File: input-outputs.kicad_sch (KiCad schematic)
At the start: 5 parts, among them J5 I2C-STEMMA-QT, J7 swd, J9 UART

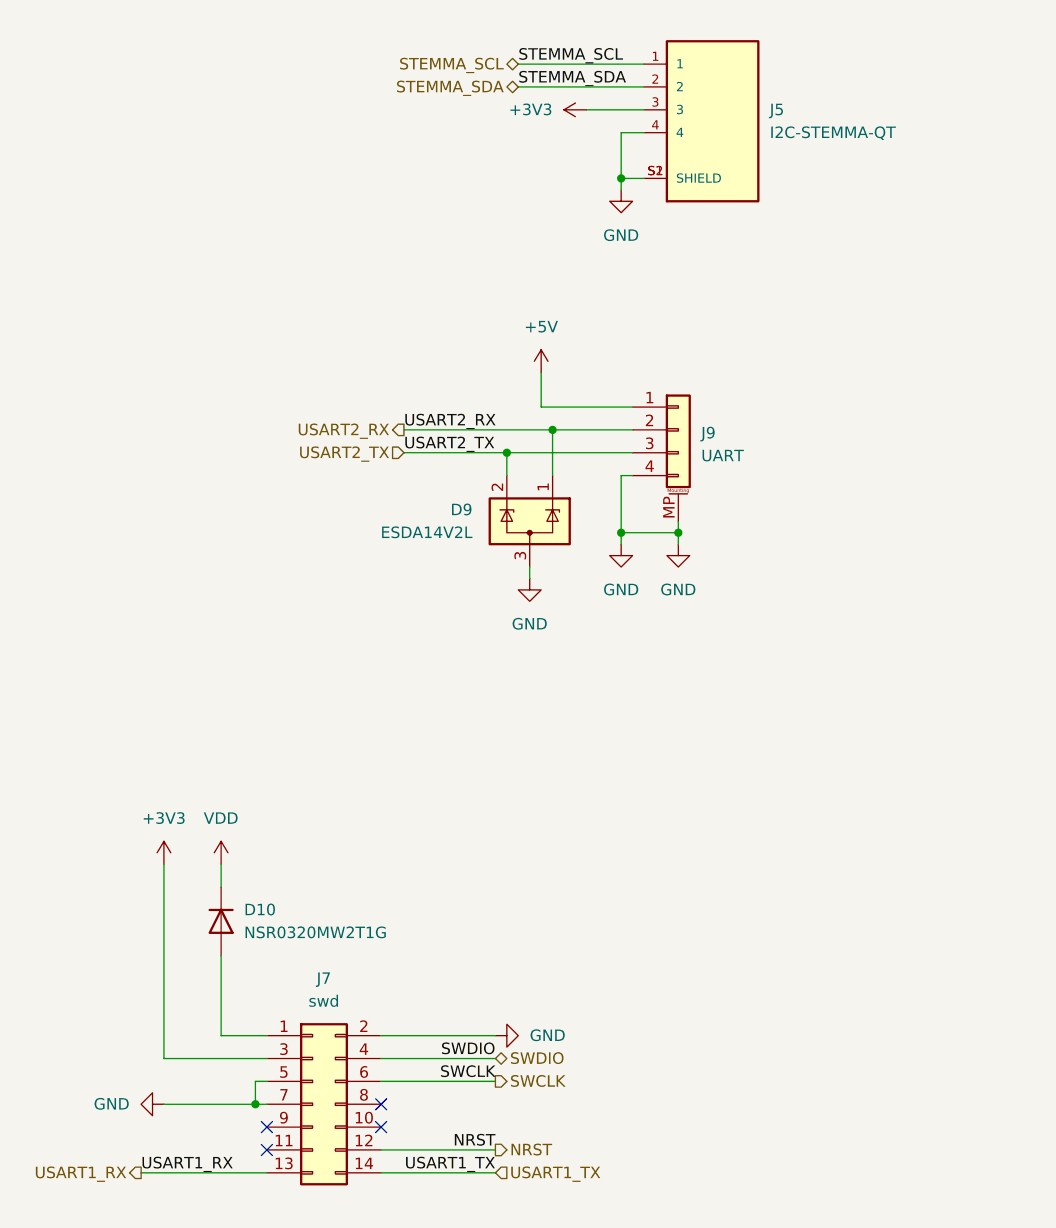
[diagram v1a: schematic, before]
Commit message: Cleaning schematic, added more independently schematics
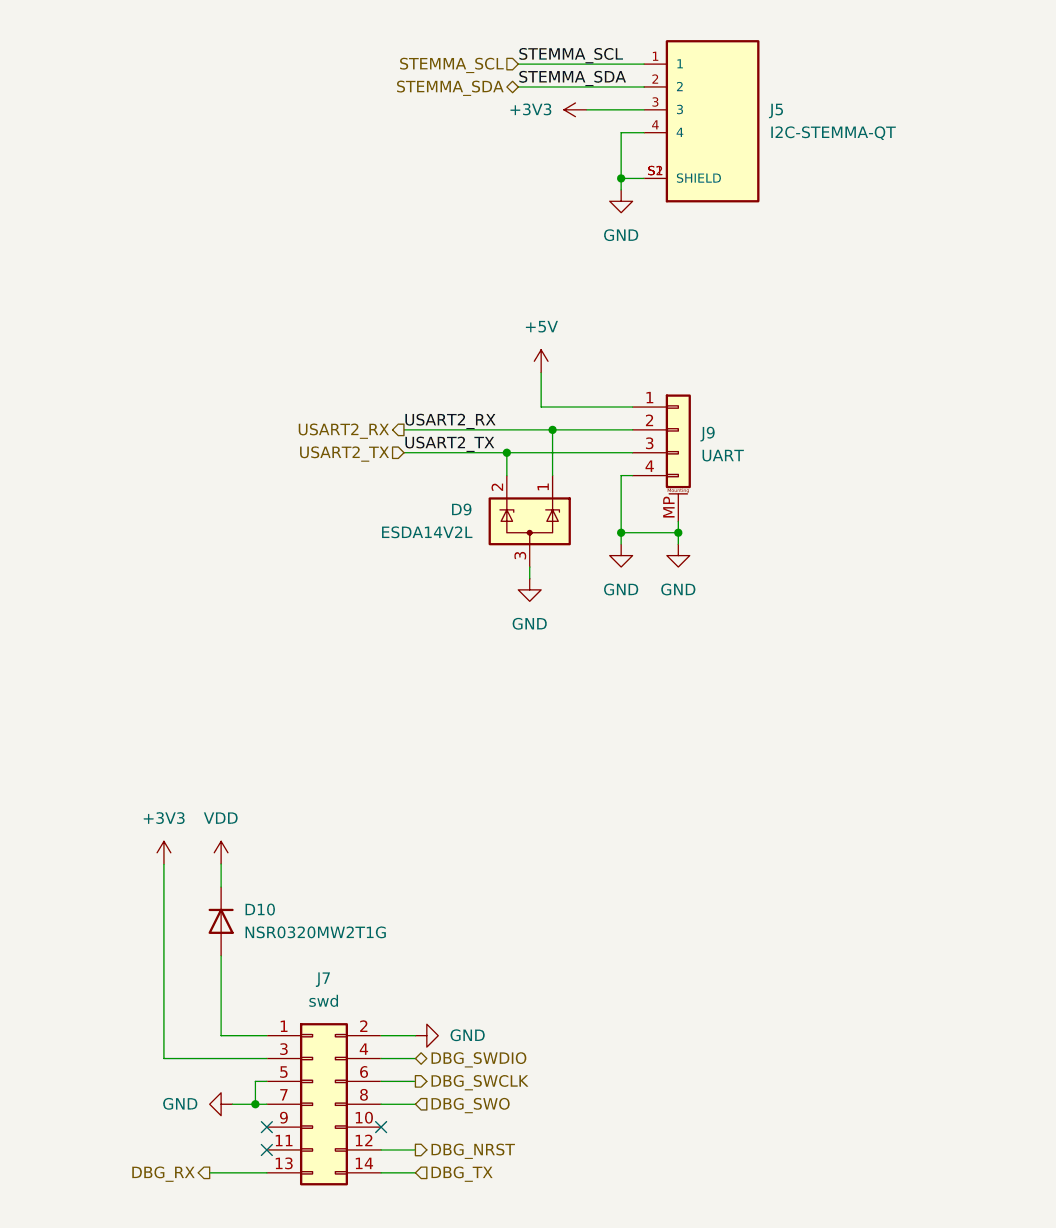
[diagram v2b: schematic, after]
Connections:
- net DBG_SWO: now reaches J7.8 (Pin_8)
- net NRST renamed DBG_NRST
- net SWCLK renamed DBG_SWCLK
- net SWDIO renamed DBG_SWDIO
- net USART1_RX renamed DBG_RX
- net USART1_TX renamed DBG_TX
- no-connect marks 4 -> 3
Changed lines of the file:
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@@
-	)
-	(no_connect
-		(at 57.15 149.86)
 	)
 	(no_connect
@@
 	(wire
 		(pts
-			(xy 57.15 157.48) (xy 69.85 157.48)
+			(xy 57.15 157.48) (xy 60.96 157.48)
 		)
 		(stroke
@@
 	(wire
 		(pts
-			(xy 57.15 144.78) (xy 69.85 144.78)
+			(xy 57.15 144.78) (xy 60.96 144.78)
 		)
 		(stroke
@@
 	(wire
 		(pts
-			(xy 57.15 154.94) (xy 69.85 154.94)
-		)
-		(stroke
-			(width 0)
-			(type default)
-		)
-	)
-	(wire
-		(pts
-			(xy 33.02 149.86) (xy 43.18 149.86)
+			(xy 57.15 154.94) (xy 60.96 154.94)
+		)
+		(stroke
+			(width 0)
+			(type default)
+		)
+	)
+	(wire
+		(pts
+			(xy 40.64 149.86) (xy 43.18 149.86)
 		)
 		(stroke
@@
 	(wire
 		(pts
-			(xy 30.48 157.48) (xy 44.45 157.48)
+			(xy 38.1 157.48) (xy 44.45 157.48)
 		)
 		(stroke
@@
 	(wire
 		(pts
+			(xy 57.15 149.86) (xy 60.96 149.86)
+		)
+		(stroke
+			(width 0)
+			(type default)
+		)
+	)
+	(wire
+		(pts
 			(xy 73.66 91.44) (xy 73.66 90.17)
 		)
@@
 	(wire
 		(pts
-			(xy 57.15 142.24) (xy 69.85 142.24)
+			(xy 57.15 142.24) (xy 60.96 142.24)
 		)
 		(stroke
@@
 	(wire
 		(pts
-			(xy 57.15 147.32) (xy 69.85 147.32)
+			(xy 57.15 147.32) (xy 60.96 147.32)
 		)
 		(stroke
@@
 		)
 	)
-	(label "SWCLK"
-		(at 69.85 147.32 180)
+	(label "STEMMA_SCL"
+		(at 72.39 34.29 0)
 		(fields_autoplaced yes)
 		(effects
@@
 				(size 1.27 1.27)
 			)
-			(justify right bottom)
-		)
-	)
-	(label "STEMMA_SCL"
-		(at 72.39 34.29 0)
+			(justify left bottom)
+		)
+	)
+	(label "USART2_TX"
+		(at 59.69 77.47 0)
 		(fields_autoplaced yes)
 		(effects
@@
 		)
 	)
-	(label "USART2_TX"
-		(at 59.69 77.47 0)
+	(label "USART2_RX"
+		(at 59.69 74.93 0)
 		(fields_autoplaced yes)
 		(effects
@@
 		)
 	)
-	(label "USART2_RX"
-		(at 59.69 74.93 0)
+	(label "STEMMA_SDA"
+		(at 72.39 36.83 0)
 		(fields_autoplaced yes)
 		(effects
@@
 		)
 	)
-	(label "SWDIO"
-		(at 69.85 144.78 180)
+	(hierarchical_label "DBG_SWO"
+		(shape input)
+		(at 60.96 149.86 0)
 		(fields_autoplaced yes)
 		(effects
@@
 				(size 1.27 1.27)
 			)
-			(justify right bottom)
-		)
-	)
-	(label "NRST"
-		(at 69.85 154.94 180)
+			(justify left)
+		)
+	)
+	(hierarchical_label "USART2_TX"
+		(shape input)
+		(at 59.69 77.47 180)
 		(fields_autoplaced yes)
 		(effects
@@
 				(size 1.27 1.27)
 			)
-			(justify right bottom)
-		)
-	)
-	(label "STEMMA_SDA"
-		(at 72.39 36.83 0)
+			(justify right)
+		)
+	)
+	(hierarchical_label "STEMMA_SCL"
+		(shape input)
+		(at 72.39 34.29 180)
 		(fields_autoplaced yes)
 		(effects
@@
 				(size 1.27 1.27)
 			)
-			(justify left bottom)
-		)
-	)
-	(label "USART1_RX"
-		(at 30.48 157.48 0)
+			(justify right)
+		)
+	)
+	(hierarchical_label "DBG_SWDIO"
+		(shape bidirectional)
+		(at 60.96 144.78 0)
 		(fields_autoplaced yes)
 		(effects
@@
 				(size 1.27 1.27)
 			)
-			(justify left bottom)
-		)
-	)
-	(label "USART1_TX"
-		(at 69.85 157.48 180)
+			(justify left)
+		)
+	)
+	(hierarchical_label "DBG_RX"
+		(shape output)
+		(at 38.1 157.48 180)
 		(fields_autoplaced yes)
 		(effects
@@
 				(size 1.27 1.27)
 			)
-			(justify right bottom)
-		)
-	)
-	(hierarchical_label "USART2_TX"
-		(shape input)
-		(at 59.69 77.47 180)
+			(justify right)
+		)
+	)
+	(hierarchical_label "DBG_SWCLK"
+		(shape output)
+		(at 60.96 147.32 0)
 		(fields_autoplaced yes)
 		(effects
@@
 				(size 1.27 1.27)
 			)
-			(justify right)
-		)
-	)
-	(hierarchical_label "STEMMA_SCL"
-		(shape bidirectional)
-		(at 72.39 34.29 180)
+			(justify left)
+		)
+	)
+	(hierarchical_label "DBG_TX"
+		(shape input)
+		(at 60.96 157.48 0)
 		(fields_autoplaced yes)
 		(effects
@@
 				(size 1.27 1.27)
 			)
-			(justify right)
-		)
-	)
-	(hierarchical_label "SWDIO"
-		(shape bidirectional)
-		(at 69.85 144.78 0)
+			(justify left)
+		)
+	)
+	(hierarchical_label "USART2_RX"
+		(shape output)
+		(at 59.69 74.93 180)
 		(fields_autoplaced yes)
 		(effects
@@
 				(size 1.27 1.27)
 			)
-			(justify left)
-		)
-	)
-	(hierarchical_label "USART1_RX"
-		(shape output)
-		(at 30.48 157.48 180)
+			(justify right)
+		)
+	)
+	(hierarchical_label "STEMMA_SDA"
+		(shape bidirectional)
+		(at 72.39 36.83 180)
 		(fields_autoplaced yes)
 		(effects
@@
 		)
 	)
-	(hierarchical_label "SWCLK"
+	(hierarchical_label "DBG_NRST"
 		(shape output)
-		(at 69.85 147.32 0)
-		(fields_autoplaced yes)
-		(effects
-			(font
-				(size 1.27 1.27)
-			)
-			(justify left)
-		)
-	)
-	(hierarchical_label "USART1_TX"
-		(shape input)
-		(at 69.85 157.48 0)
-		(fields_autoplaced yes)
-		(effects
-			(font
-				(size 1.27 1.27)
-			)
-			(justify left)
-		)
-	)
-	(hierarchical_label "USART2_RX"
-		(shape output)
-		(at 59.69 74.93 180)
-		(fields_autoplaced yes)
-		(effects
-			(font
-				(size 1.27 1.27)
-			)
-			(justify right)
-		)
-	)
-	(hierarchical_label "STEMMA_SDA"
-		(shape bidirectional)
-		(at 72.39 36.83 180)
-		(fields_autoplaced yes)
-		(effects
-			(font
-				(size 1.27 1.27)
-			)
-			(justify right)
-		)
-	)
-	(hierarchical_label "NRST"
-		(shape output)
-		(at 69.85 154.94 0)
+		(at 60.96 154.94 0)
 		(fields_autoplaced yes)
 		(effects
@@
 		(lib_name "GND_3")
 		(lib_id "power:GND")
-		(at 69.85 142.24 90)
+		(at 60.96 142.24 90)
 		(mirror x)
 		(unit 1)
@@
 		(fields_autoplaced yes)
 		(property "Reference" "#PWR0117"
-			(at 76.2 142.24 0)
+			(at 67.31 142.24 0)
 			(effects
 				(font
@@
 		)
 		(property "Value" "GND"
-			(at 73.66 142.2399 90)
+			(at 64.77 142.2399 90)
 			(effects
 				(font
@@
 		)
 		(property "Footprint" ""
-			(at 69.85 142.24 0)
+			(at 60.96 142.24 0)
 			(effects
 				(font
@@
 		)
 		(property "Datasheet" ""
-			(at 69.85 142.24 0)
+			(at 60.96 142.24 0)
 			(effects
 				(font
@@
 		)
 		(property "Description" "Power symbol creates a global label with name \"GND\" , ground"
-			(at 69.85 142.24 0)
+			(at 60.96 142.24 0)
 			(effects
 				(font
@@
 		(lib_name "GND_3")
 		(lib_id "power:GND")
-		(at 33.02 149.86 270)
+		(at 40.64 149.86 270)
 		(unit 1)
 		(exclude_from_sim no)
@@
 		(fields_autoplaced yes)
 		(property "Reference" "#PWR0116"
-			(at 26.67 149.86 0)
+			(at 34.29 149.86 0)
 			(effects
 				(font
@@
 		)
 		(property "Value" "GND"
-			(at 29.21 149.8599 90)
+			(at 36.83 149.8599 90)
 			(effects
 				(font
@@
 		)
 		(property "Footprint" ""
-			(at 33.02 149.86 0)
+			(at 40.64 149.86 0)
 			(effects
 				(font
@@
 		)
 		(property "Datasheet" ""
-			(at 33.02 149.86 0)
+			(at 40.64 149.86 0)
 			(effects
 				(font
@@
 		)
 		(property "Description" "Power symbol creates a global label with name \"GND\" , ground"
-			(at 33.02 149.86 0)
-			(effects
-				(font
+			(at 40.64 149.86 0)
+			(effects
+				(font

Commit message: Finished SDRAM, QSPI Flash, Planning to move to 5 inch orient display dimension
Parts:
- D10: JLCPCB Part # (none) -> C48192
- D9: JLCPCB Part # (none) -> C343996
- J7: JLCPCB Part # (none) -> C2881912
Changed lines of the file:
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@@
+			)
+		)
+		(property "JLCPCB Part #" "C2881912"
+			(at 49.53 149.86 0)
+			(effects
+				(font
+					(size 1.27 1.27)
+				)
+				(hide yes)
 			)
 		)
@@
 		)
 		(property "Sim.Pins" "1=K 2=A"
+			(at 39.37 129.54 0)
+			(effects
+				(font
+					(size 1.27 1.27)
+				)
+				(hide yes)
+			)
+		)
+		(property "JLCPCB Part #" "C48192"
 			(at 39.37 129.54 0)
 			(effects
@@
 			(at 73.66 85.09 0)
 			(effects
+				(font
+					(size 1.27 1.27)
+				)
+				(hide yes)
+			)
+		)
+		(property "JLCPCB Part #" "C343996"
+			(at 73.66 85.09 0)
+			(effects

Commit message: not yet
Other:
- note added: "TO MCU RX"
- note added: "TO MCU TX"
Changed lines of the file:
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@@
+		)
+	)
+	(text "TO MCU TX"
+		(exclude_from_sim no)
+		(at 65.024 160.528 0)
+		(effects
+			(font
+				(size 1.27 1.27)
+			)
+		)
+	)
+	(text "TO MCU RX"
+		(exclude_from_sim no)
+		(at 34.544 160.528 0)
+		(effects
+			(font
+				(size 1.27 1.27)
+			)
 		)
 	)

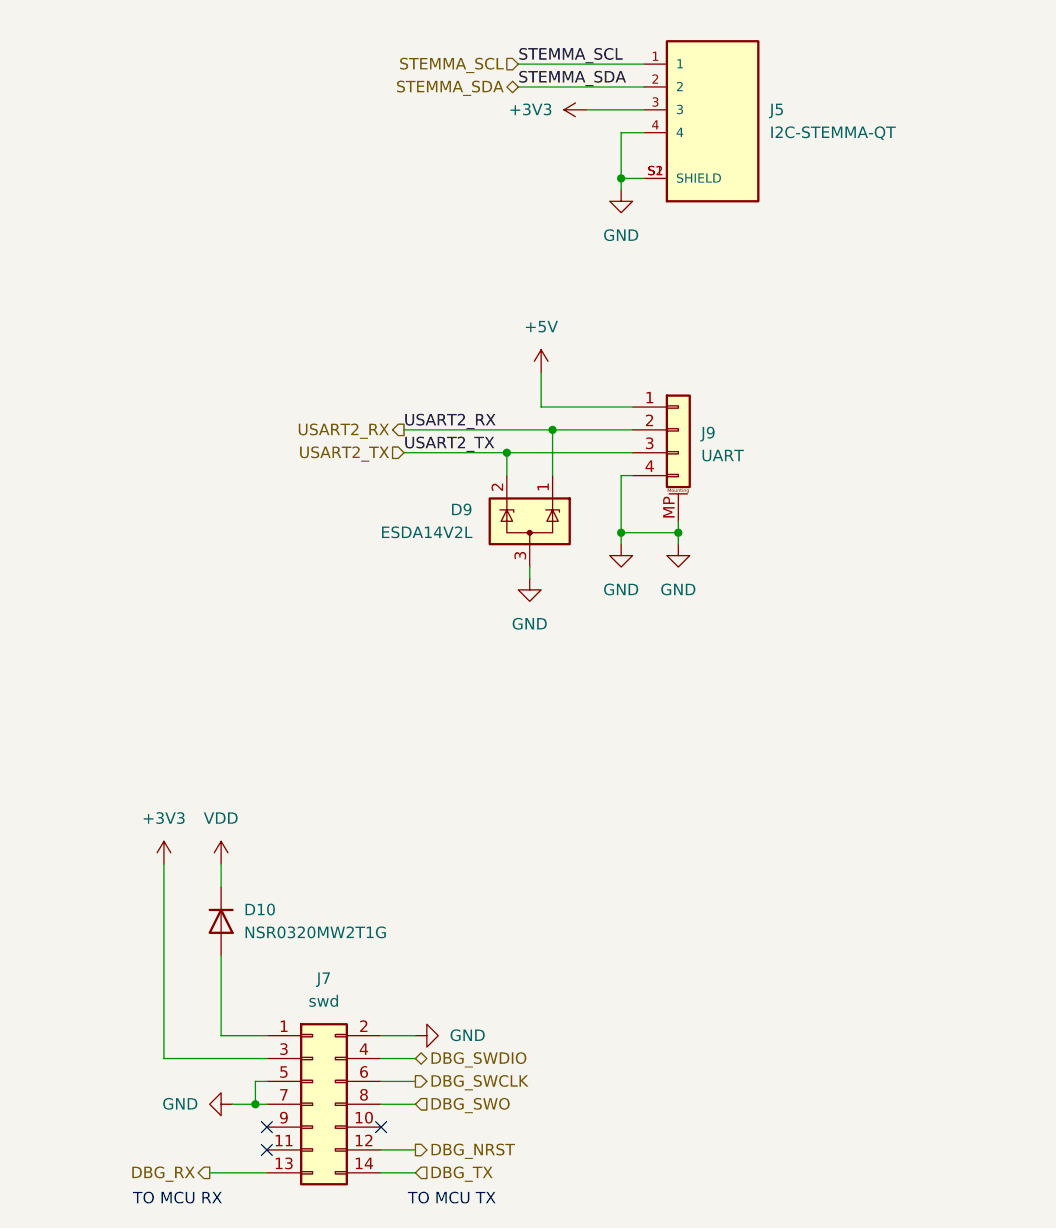
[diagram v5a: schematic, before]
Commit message: Button, LED, i2s audio, LCD & SD ctrl left
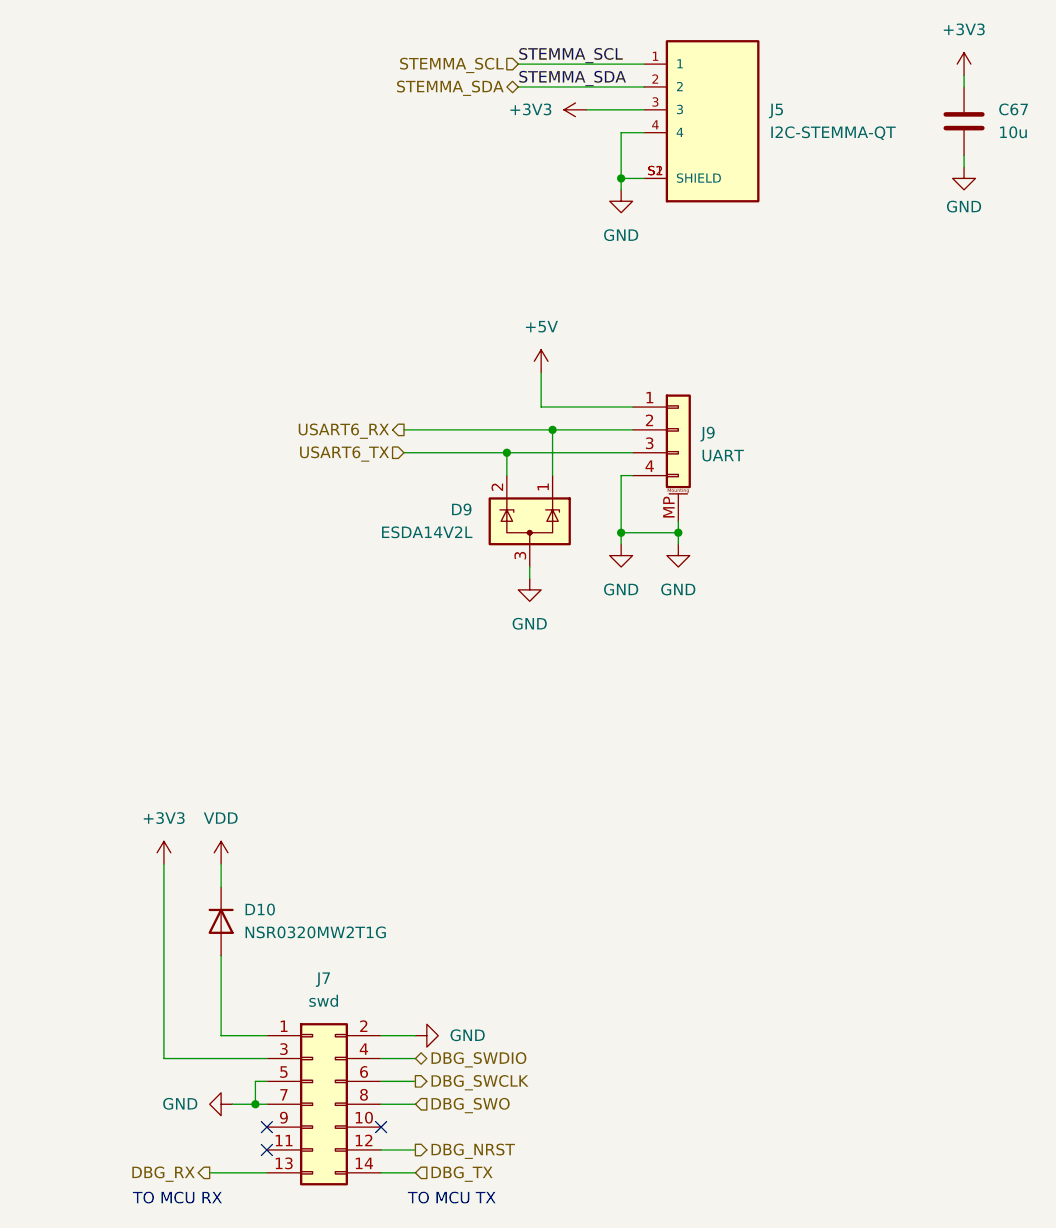
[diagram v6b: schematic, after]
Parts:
- added C67: 10u, Capacitor_SMD:C_0603_1608Metric, symbol Device:C
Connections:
- net +3V3: now also C67.1
- net GND: now also C67.2
- net USART2_RX renamed USART6_RX
- net USART2_TX renamed USART6_TX

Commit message: Almost finished
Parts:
- J9: JLCPCB Part # C146120 -> C7430470
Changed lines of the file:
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@@
 			)
 		)
-		(property "JLCPCB Part #" "C146120"
+		(property "JLCPCB Part #" "C7430470"
 			(at 90.17 74.93 0)
 			(effects
